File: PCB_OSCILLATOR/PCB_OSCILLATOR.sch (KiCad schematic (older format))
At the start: 100 parts, among them J1 Jumper, J10 Jumper, J11 Jumper, J12 Jumper, J13 Jumper, J14 Jumper, J15 Jumper, J16 Jumper, J2 Jumper, J3 Jumper, J4 Jumper, J5 Jumper, J6 Jumper, J7 Jumper, J8 Jumper, J9 Jumper, P1 CONN_01X04, P2 MCLK_EXTERNAL, P3 SPI_AD5270_1, P4 SPI_AD5270_2, P5 SPI_AD9833_1, P6 SPI_AD9833_2, P7 CONN_01X04, U1 AD5270, U10 ADR291, U2 AD8421, U3 AD9833, U4 AD5270, U5 AD8421, U6 AD9833, U7 ADG819, U8 ADP3303, U9 AD8651

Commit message: PCB 95%
Terminar de hacer planos que se crean convenientes//
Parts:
- removed C33, C37: 0.1uF, Capacitors_SMD:C_0805_HandSoldering, symbol 0.1uF
- removed C36, C38: 10uF, Capacitors_SMD:C_0805_HandSoldering, symbol 10uF
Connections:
- net +12V: now also P7.2 (P2); no longer P7.1 (P1)
- net -12V: now also P7.1 (P1), P7.3 (P3); no longer P7.2 (P2)
- net GND: no longer P7.3 (P3)
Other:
- moved on the sheet: C28, C29, D1, D2, D3, P7, R12, R13, R14

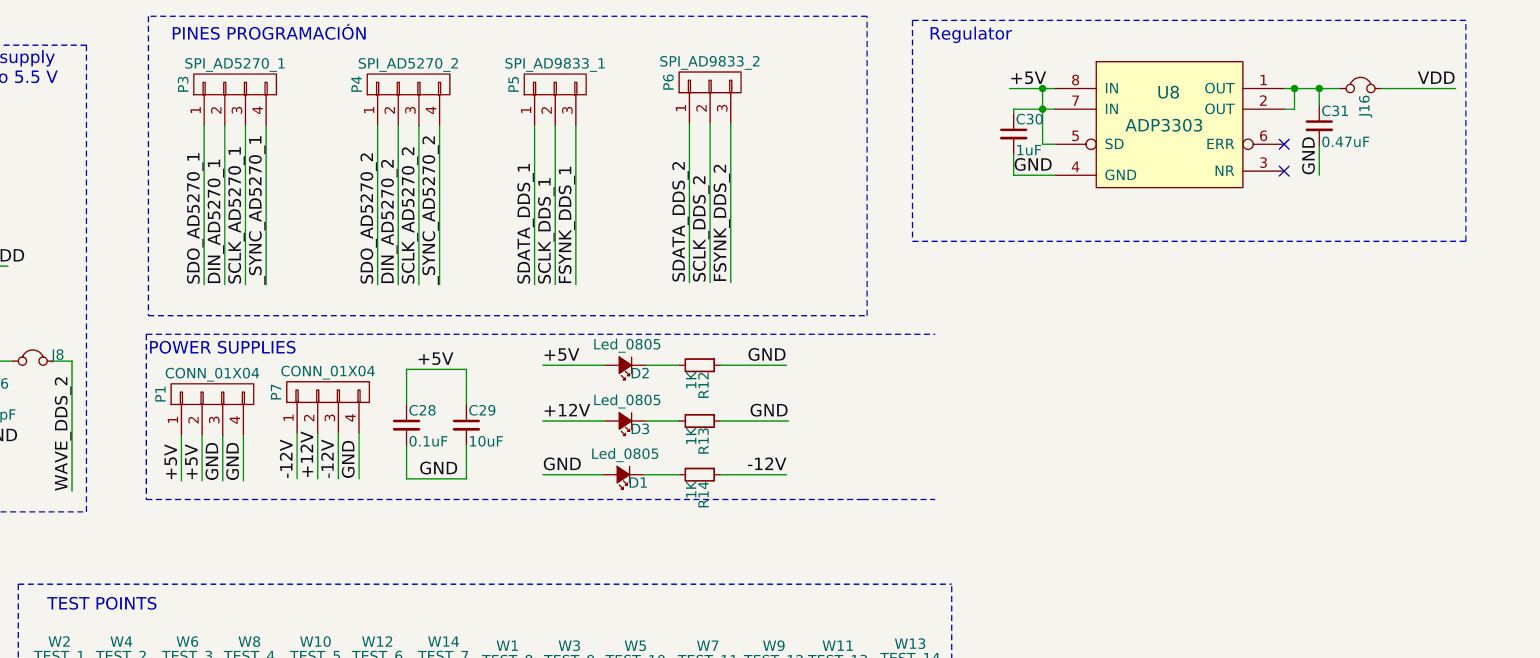
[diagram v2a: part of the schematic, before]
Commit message: Cambio de regulador en esquematico
//
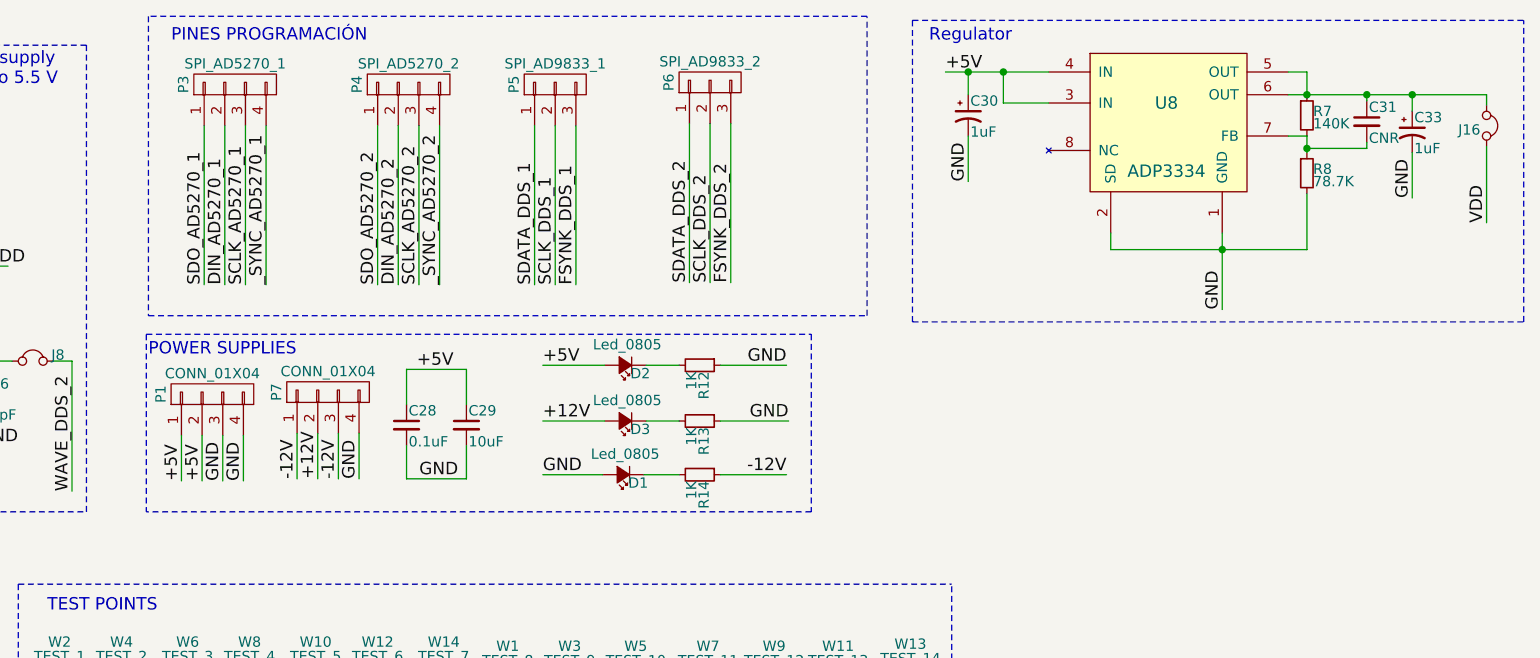
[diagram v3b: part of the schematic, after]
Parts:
- removed C30: 1uF, Capacitors_SMD:C_0805_HandSoldering, symbol 1uF
- removed C31: 0.47uF, Capacitors_SMD:C_1206_HandSoldering, symbol 0.47uF
- removed U8: ADP3303, Housings_SOIC:SOIC-8_3.9x4.9mm_Pitch1.27mm, symbol ADP3303
- added C30, C33: 1uF, Capacitors_SMD:C_0805_HandSoldering, symbol CP1_Small
- added C31: CNR, Capacitors_SMD:C_1206_HandSoldering, symbol C_Small
- added R7: 140K, symbol R_Small
- added R8: 78.7K, symbol R_Small
- added U8: ADP3334, Housings_SOIC:SOIC-8_3.9x4.9mm_Pitch1.27mm, symbol ADP3334
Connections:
- net +5V: now also C30.1, U8.3 (IN), U8.4 (IN)
- net GND: now also C30.2, C33.2, R8.2, U8.1 (GND), U8.2 (SD)
- net at J16.2: now also C31.1, C33.1, R7.1, U8.5 (OUT), U8.6 (OUT)
- new net: C31.2, R7.2, R8.1, U8.7 (FB)
- no-connect marks 4 -> 2
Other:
- moved on the sheet: J16
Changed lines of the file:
@@
 Text Label 6080 9390 2    60   ~ 0
 GND
-NoConn ~ 12990 1440
-NoConn ~ 12990 1310
-Text Label 13820 1040 2    60   ~ 0
+Text Label 13970 1690 1    60   ~ 0
 VDD
-Text Label 11680 1460 0    60   ~ 0
-GND
-Text Label 11660 1040 0    60   ~ 0
+Text Label 11350 960  0    60   ~ 0
 +5V
-Text Label 13160 1460 1    60   ~ 0
-GND
 Wire Wire Line
 	1470 1980 2080 1980
@@
 	8920 3990 8920 4930
 Wire Notes Line
-	7480 2230 7480 3030
-Wire Notes Line
-	7480 3030 10960 3030
-Wire Notes Line
-	7480 2230 11300 2230
+	7480 2230 7480 3090
 Wire Wire Line
 	9400 2380 9700 2380
@@
 	5530 9390 5430 9390
 Connection ~ 5430 9390
-Wire Wire Line
-	11820 1310 11880 1310
-Wire Wire Line
-	11820 1040 11820 1310
-Wire Wire Line
-	11660 1040 11880 1040
-Wire Wire Line
-	11680 1140 11880 1140
-Connection ~ 11820 1140
-Connection ~ 11820 1040
-Wire Wire Line
-	12990 1140 13040 1140
-Wire Wire Line
-	13040 1140 13040 1040
-Wire Wire Line
-	12990 1040 13260 1040
-Connection ~ 13040 1040
-Wire Wire Line
-	11680 1460 11880 1460
-Wire Wire Line
-	13160 1120 13160 1040
-Connection ~ 13160 1040
-Wire Wire Line
-	13160 1320 13160 1460
-Wire Wire Line
-	11680 1140 11680 1160
-Wire Wire Line
-	11680 1460 11680 1360
 Wire Notes Line
 	11190 710  11190 1780
 Wire Notes Line
-	11190 1780 13870 1780
-Wire Notes Line
-	13870 1780 13870 710
-Wire Notes Line
-	13870 710  11190 710
+	11190 710  14150 710
 Text Notes 11270 820  0    60   ~ 0
 Regulator
@@
 Wire Wire Line
 	5410 4990 5410 5020
-Wire Notes Line
-	10950 3030 11300 3030
 $Comp
 L 1K R3
@@
 Wire Notes Line
 	6650 9230 3580 9230
-Wire Wire Line
-	13460 1040 13820 1040
 $Comp
 L ADG819 U7
@@
 F 3 "" H 7840 6890 60  0000 C CNN
 	1    7840 6890
-	1    0    0    -1
-$EndComp
-$Comp
-L ADP3303 U8
-U 1 1 59260242
-P 12350 1120
-F 0 "U8" H 12430 1180 60  0000 C CNN
-F 1 "ADP3303" H 12410 1020 60  0000 C CNN
-F 2 "Housings_SOIC:SOIC-8_3.9x4.9mm_Pitch1.27mm" H 12330 1080 60  0001 C CNN
-F 3 "" H 12350 1120 60  0000 C CNN
-	1    12350 1120
 	1    0    0    -1
 $EndComp
@@
 Wire Wire Line
 	11180 4000 11180 4940
-$Comp
-L 0.47uF C31
-U 1 1 59278D51
-P 13160 1220
-F 0 "C31" H 13170 1290 50  0000 L CNN
-F 1 "0.47uF" H 13170 1140 50  0000 L CNN
-F 2 "Capacitors_SMD:C_1206_HandSoldering" H 13070 1190 50  0001 C CNN
-F 3 "" H 13170 1290 50  0000 C CNN
-F 4 "399-3695-1-ND" H 13270 1390 60  0001 C CNN "0.47µF ±10% Molded Tantalum Capacitors 25V 1206 (3216 Metric) 14 Ohm"
-	1    13160 1220
-	1    0    0    -1
-$EndComp
-$Comp
-L 1uF C30
-U 1 1 5927AA83
-P 11680 1260
-F 0 "C30" H 11690 1330 50  0000 L CNN
-F 1 "1uF" H 11690 1180 50  0000 L CNN
-F 2 "Capacitors_SMD:C_0805_HandSoldering" H 11590 1230 50  0001 C CNN
-F 3 "" H 11690 1330 50  0000 C CNN
-F 4 "478-8126-2-ND" H 11790 1430 60  0001 C CNN "CAP TANT 1UF 16V 20% 0805"
-	1    11680 1260
-	1    0    0    -1
-$EndComp
 Wire Notes Line
 	9160 5060 11380 5060
@@
 L Jumper J16
 U 1 1 591BCCCA
-P 13360 1040
-F 0 "J16" H 13390 1060 50  0000 L CNN
-F 1 "Jumper" H 13390 1000 50  0001 L CNN
-F 2 "Pin_Headers:Pin_Header_Straight_1x02" H 13290 960 50  0001 C CNN
-F 3 "" H 13360 1040 50  0000 C CNN
-	1    13360 1040
-	0    1    1    0
+P 13970 1220
+F 0 "J16" H 14000 1240 50  0000 L CNN
+F 1 "Jumper" H 14000 1180 50  0001 L CNN
+F 2 "Pin_Headers:Pin_Header_Straight_1x02" H 13900 1140 50  0001 C CNN
+F 3 "" H 13970 1220 50  0000 C CNN
+	1    13970 1220
+	-1   0    0    1
 $EndComp
 $Comp
@@
 Text Label 8210 2930 1    60   ~ 0
 -12V
+Wire Wire Line
+	11630 1110 11630 960
+Wire Wire Line
+	11350 960  11850 960
+Connection ~ 11630 960
+$Comp
+L CP1_Small C30
+U 1 1 591E58AE
+P 11460 1170
+F 0 "C30" H 11470 1240 50  0000 L CNN
+F 1 "1uF" H 11470 1090 50  0000 L CNN
+F 2 "Capacitors_SMD:C_0805_HandSoldering" H 11460 1170 50  0001 C CNN
+F 3 "" H 11460 1170 50  0000 C CNN
+	1    11460 1170
+	1    0    0    -1
+$EndComp
+Wire Wire Line
+	11460 1070 11460 960
+Connection ~ 11460 960
+Wire Wire Line
+	11460 1270 11460 1490
+Text Label 11460 1490 1    60   ~ 0
+GND
+Wire Wire Line
+	12690 1740 12690 2110
+Text Label 12690 2110 1    60   ~ 0
+GND
+$Comp
+L ADP3334 U8
+U 1 1 591FDE16
+P 12410 1220
+F 0 "U8" H 12420 1330 60  0000 C CNN
+F 1 "ADP3334" H 12420 1000 60  0000 C CNN
+F 2 "Housings_SOIC:SOIC-8_3.9x4.9mm_Pitch1.27mm" H 12410 1130 60  0001 C CNN
+F 3 "" H 12410 1130 60  0000 C CNN
+	1    12410 1220
+	1    0    0    -1
+$EndComp
+Wire Wire Line
+	11850 1110 11630 1110
+Wire Wire Line
+	12150 1740 12150 1820
+Wire Wire Line
+	12150 1820 13100 1820
+Connection ~ 12690 1820
+$Comp
+L R_Small R7
+U 1 1 59206466
+P 13100 1170
+F 0 "R7" H 13130 1190 50  0000 L CNN
+F 1 "140K" H 13130 1130 50  0000 L CNN
+F 2 "" H 13100 1170 50  0001 C CNN
+F 3 "" H 13100 1170 50  0000 C CNN
+	1    13100 1170
+	1    0    0    -1
+$EndComp
+Wire Wire Line
+	13100 1270 13010 1270
+$Comp
+L R_Small R8
+U 1 1 5920981F
+P 13100 1450
+F 0 "R8" H 13130 1470 50  0000 L CNN
+F 1 "78.7K" H 13130 1410 50  0000 L CNN
+F 2 "" H 13100 1450 50  0001 C CNN
+F 3 "" H 13100 1450 50  0000 C CNN
+	1    13100 1450
+	1    0    0    -1
+$EndComp
+Wire Wire Line
+	13100 1350 13100 1270
+Wire Wire Line
+	13100 1820 13100 1550
+Connection ~ 13100 1070
+Wire Wire Line
+	13010 960  13100 960
+Wire Wire Line
+	13100 960  13100 1070
+Wire Notes Line
+	11190 1770 11190 2170
+Wire Notes Line
+	11190 2170 14150 2170
+Wire Notes Line
+	14150 2170 14150 710
+Wire Notes Line
+	7480 2230 10700 2230
+Wire Notes Line
+	10700 2230 10700 3090
+Wire Notes Line
+	10700 3090 7480 3090
+$Comp
+L C_Small C31
+U 1 1 591DC897
+P 13390 1200
+F 0 "C31" H 13400 1270 50  0000 L CNN
+F 1 "CNR" H 13400 1120 50  0000 L CNN
+F 2 "Capacitors_SMD:C_1206_HandSoldering" H 13390 1200 50  0001 C CNN
+F 3 "" H 13390 1200 50  0000 C CNN
+	1    13390 1200
+	1    0    0    -1
+$EndComp
+Wire Wire Line
+	13390 1100 13390 1070
+Connection ~ 13390 1070
+Wire Wire Line
+	13390 1300 13390 1330
+Wire Wire Line
+	13390 1330 13100 1330
+Connection ~ 13100 1330
+$Comp
+L CP1_Small C33
+U 1 1 591E24B2
+P 13610 1250
+F 0 "C33" H 13620 1320 50  0000 L CNN
+F 1 "1uF" H 13620 1170 50  0000 L CNN
+F 2 "Capacitors_SMD:C_0805_HandSoldering" H 13610 1250 50  0001 C CNN
+F 3 "" H 13610 1250 50  0000 C CNN
+	1    13610 1250
+	1    0    0    -1
+$EndComp
+Wire Wire Line
+	13610 1350 13610 1570
+Text Label 13610 1570 1    60   ~ 0
+GND
+Wire Wire Line
+	13610 1150 13610 1070
+Connection ~ 13610 1070
+Wire Wire Line
+	13010 1070 13970 1070
+Wire Wire Line
+	13970 1320 13970 1690
+Wire Wire Line
+	13970 1070 13970 1120
 $EndSCHEMATC

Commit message: //
//
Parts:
- J1, J10, J11, J12, J13, J14, J15, J16, J2, J3, J4, J5, J6, J7, J8, J9: symbol Jumper -> Jumper-RESCUE-PCB_OSCILLATOR
- R7, R8: footprint (none) -> Resistors_SMD:R_0805_HandSoldering
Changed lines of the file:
@@
 EESchema Schematic File Version 2
+LIBS:PCB_OSCILLATOR-rescue
 LIBS:power
 LIBS:device
@@
 GAIN VARIABLE\nAMPLIFIER_2
 $Comp
-L Jumper J1
+L Jumper-RESCUE-PCB_OSCILLATOR J1
 U 1 1 59183800
 P 1630 4420
@@
 $EndComp
 $Comp
-L Jumper J2
+L Jumper-RESCUE-PCB_OSCILLATOR J2
 U 1 1 591840B8
 P 1630 4520
@@
 $EndComp
 $Comp
-L Jumper J3
+L Jumper-RESCUE-PCB_OSCILLATOR J3
 U 1 1 591877BD
 P 4430 4420
@@
 $EndComp
 $Comp
-L Jumper J4
+L Jumper-RESCUE-PCB_OSCILLATOR J4
 U 1 1 591877C3
 P 4430 4520
@@
 $EndComp
 $Comp
-L Jumper J5
+L Jumper-RESCUE-PCB_OSCILLATOR J5
 U 1 1 59196A89
 P 3090 4490
@@
 $EndComp
 $Comp
-L Jumper J7
+L Jumper-RESCUE-PCB_OSCILLATOR J7
 U 1 1 5919821A
 P 5890 4490
@@
 $EndComp
 $Comp
-L Jumper J8
+L Jumper-RESCUE-PCB_OSCILLATOR J8
 U 1 1 5919B755
 P 6930 2360
@@
 $EndComp
 $Comp
-L Jumper J6
+L Jumper-RESCUE-PCB_OSCILLATOR J6
 U 1 1 5919CAA1
 P 3870 2390
@@
 $EndComp
 $Comp
-L Jumper J11
+L Jumper-RESCUE-PCB_OSCILLATOR J11
 U 1 1 591A6097
 P 8400 6690
@@
 $EndComp
 $Comp
-L Jumper J10
+L Jumper-RESCUE-PCB_OSCILLATOR J10
 U 1 1 591B45E8
 P 1820 2610
@@
 $EndComp
 $Comp
-L Jumper J9
+L Jumper-RESCUE-PCB_OSCILLATOR J9
 U 1 1 591B4BE3
 P 1820 2430
@@
 Regulator
 $Comp
-L Jumper J14
+L Jumper-RESCUE-PCB_OSCILLATOR J14
 U 1 1 591FF1E0
 P 1510 9000
@@
 	1510 9690 1510 9640
 $Comp
-L Jumper J13
+L Jumper-RESCUE-PCB_OSCILLATOR J13
 U 1 1 5920AEAD
 P 5410 5120
@@
 $EndComp
 $Comp
-L Jumper J16
+L Jumper-RESCUE-PCB_OSCILLATOR J16
 U 1 1 591BCCCA
 P 13970 1220
@@
 $EndComp
 $Comp
-L Jumper J15
+L Jumper-RESCUE-PCB_OSCILLATOR J15
 U 1 1 591C0AC5
 P 1510 9790
@@
 $EndComp
 $Comp
-L Jumper J12
+L Jumper-RESCUE-PCB_OSCILLATOR J12
 U 1 1 591C2C1D
 P 2610 5140
@@
 F 0 "R7" H 13130 1190 50  0000 L CNN
 F 1 "140K" H 13130 1130 50  0000 L CNN
-F 2 "" H 13100 1170 50  0001 C CNN
+F 2 "Resistors_SMD:R_0805_HandSoldering" H 13100 1170 50  0001 C CNN
 F 3 "" H 13100 1170 50  0000 C CNN
 	1    13100 1170
@@
 F 0 "R8" H 13130 1470 50  0000 L CNN
 F 1 "78.7K" H 13130 1410 50  0000 L CNN
-F 2 "" H 13100 1450 50  0001 C CNN
+F 2 "Resistors_SMD:R_0805_HandSoldering" H 13100 1450 50  0001 C CNN
 F 3 "" H 13100 1450 50  0000 C CNN
 	1    13100 1450
